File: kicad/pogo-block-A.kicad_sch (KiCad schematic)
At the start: 9 parts, among them J1 L_IN, J2 R_IN, U1 OPA1612

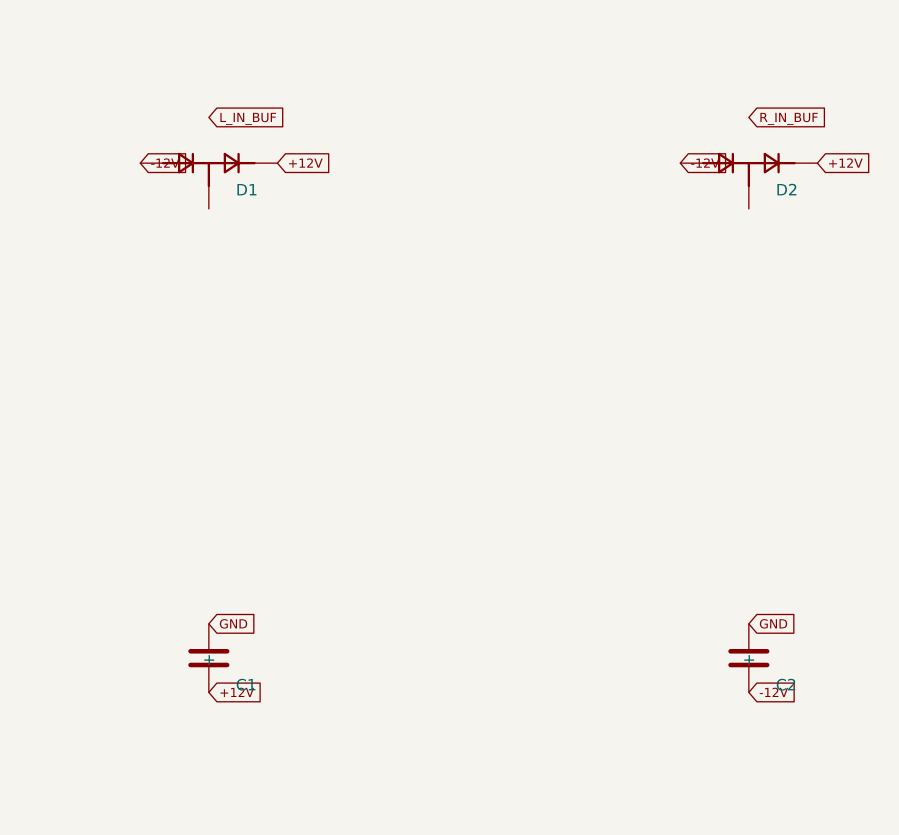
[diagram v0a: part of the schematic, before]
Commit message: 0015-component-audit: apply component verification fixes
Board-breaking:
- that2180: real MPN THAT2180AL08-U (grade A) + package SIP-8 (THT); vendor
  Package_SIP/SIP-8_2.54mm footprint; fix components.yaml U4/U5 + CLAUDE.md.
  The 2180 has no SMD/SOIC variant.
- bat54s: redraw symbol to real series topology (1=A1, 2=K2, 3=K1;A2 junction);
  swap pins 2<->3 on all 24 BAT54S instances (blocks A/1/3/4) so signal sits on the
  junction (pin3), +12V on K2 (pin2), -12V on A1 (pin1); fix aux-cv-protection.md +
  block-A spec (both mislabeled the signal node as pin 2).

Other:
- R_INV_IN/R_INV_FB: add tol 1% (header-required >60 dB null).
- slide_pot_45mm: MPN RA4522F (Alpha 45mm, Rapid/Banzai); fix datasheet link.
- bzx84c10: add shared BZX84_SER datasheet (committed PDF + sha256); canonical MPN.
- opa1612: add symbol opamp2. bourns_3296w/3224w: fix version strings.
- cd4053 symbol doc# -> SCHS047O; c.yaml pin1 '+' -> '~' (non-polarized).

Jack S/T/TN reconciliation deferred (its own change). Plugin DSP untouched.
Regenerated all schematics, BOM, fp-lib-table, footprint SVGs, panel; 5 gates green.
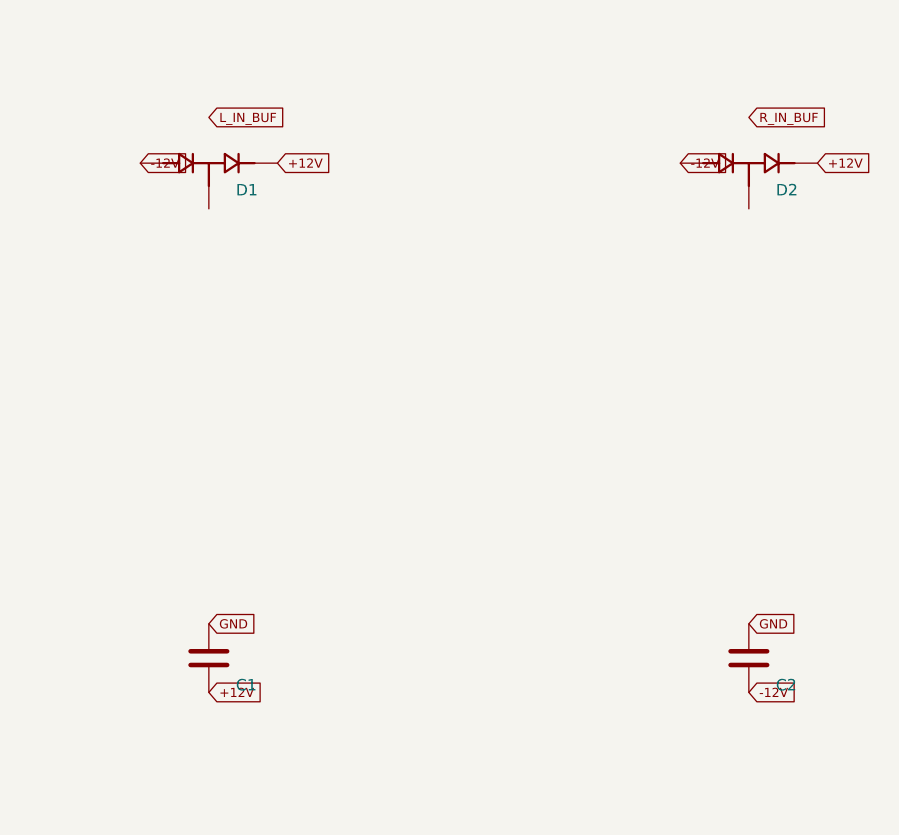
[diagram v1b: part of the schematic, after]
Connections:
- net +12V: now also D1.2 (K2), D2.2 (K2); no longer D1.3 (K2), D2.3 (K2)
